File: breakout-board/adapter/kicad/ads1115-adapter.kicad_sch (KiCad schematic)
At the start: 7 parts, among them J1 TO BOARD J15, J2 TO BOARD J10, J3 ADS1115 10-PIN

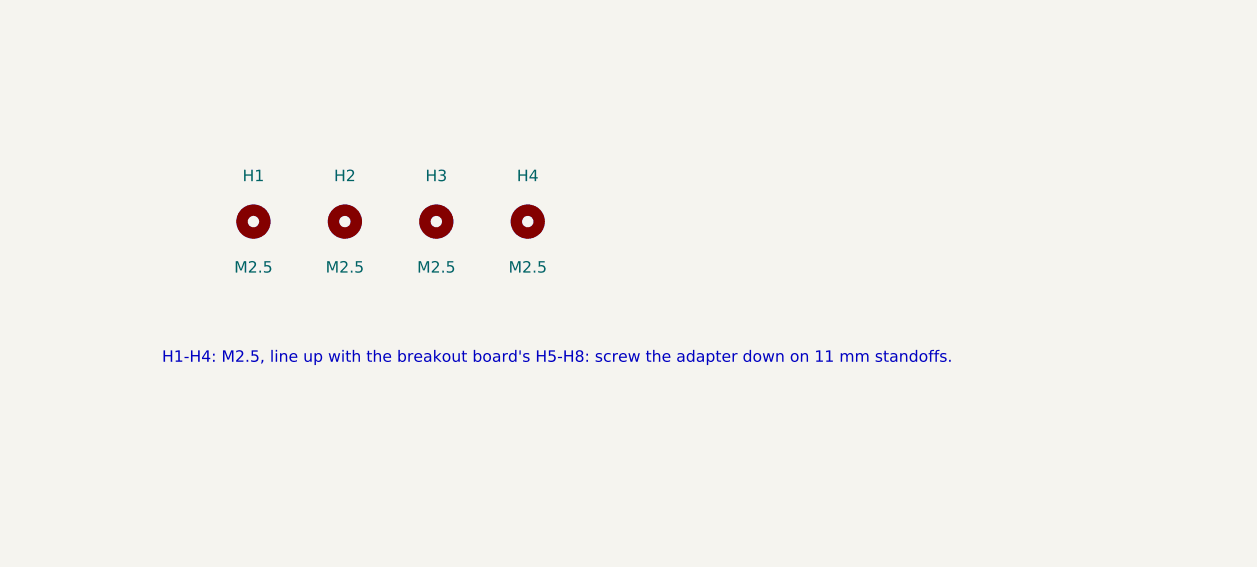
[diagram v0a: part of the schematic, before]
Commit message: Bigger logo on the breakout board; ADS1115 adapter rev 1.1 (module holes)
- Breakout board: Project Moon Pi logo 18 -> 26 mm in the top strip (silkscreen
  only, routing unchanged); Gerbers and pictures updated
- ADS1115 adapter rev 1.1: 5 mm taller (42 x 24.7 mm) with M2.5 holes H5/H6 for
  the 10-pin board's own mounting holes (original Adafruit layout), labelled on
  the silkscreen; README fitting order and parts list updated

Co-Authored-By: Claude Opus 5.5 <noreply@anthropic.com>
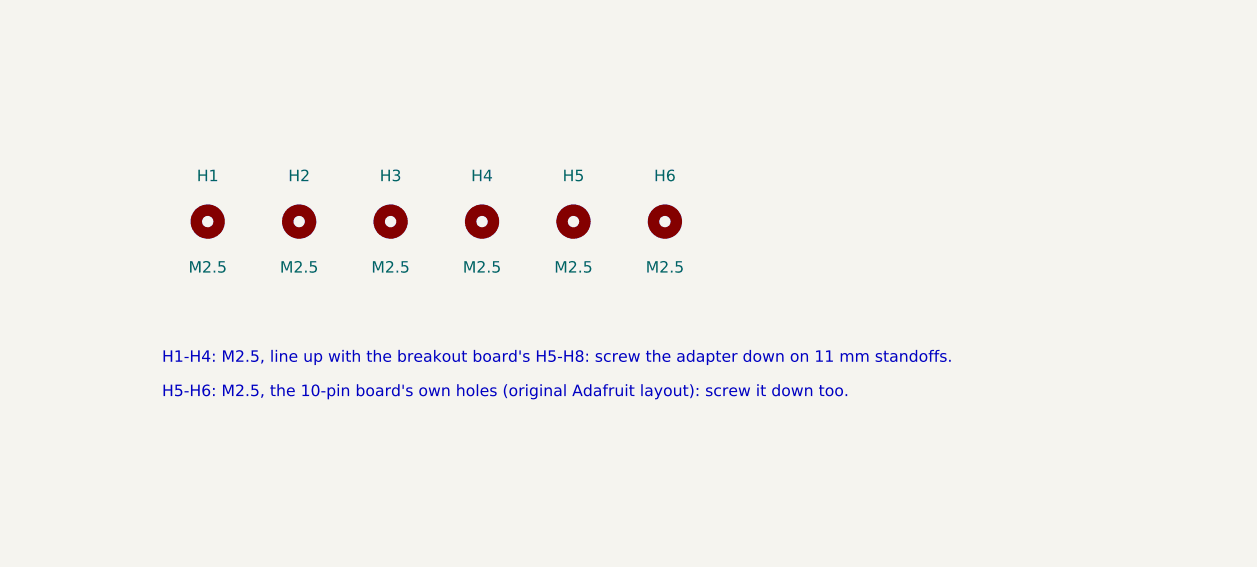
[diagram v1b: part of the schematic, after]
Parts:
- added H5, H6: M2.5, MountingHole:MountingHole_2.7mm_M2.5, symbol Mechanical:MountingHole
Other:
- note added: "H5-H6: M2.5, the 10-pin board's own holes (original Adafruit layout): screw it down too."
